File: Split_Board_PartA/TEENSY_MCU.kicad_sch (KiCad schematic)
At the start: 15 parts, among them J3 Conn_01x20, J4 Conn_01x15, U2 ADUM240E0BRWZ, U3 ADUM240E0BRWZ, U37 MYTEENSY_SYMBOL, U42 ADUM241E1BRIZ, U5 ADUM240E0BRWZ

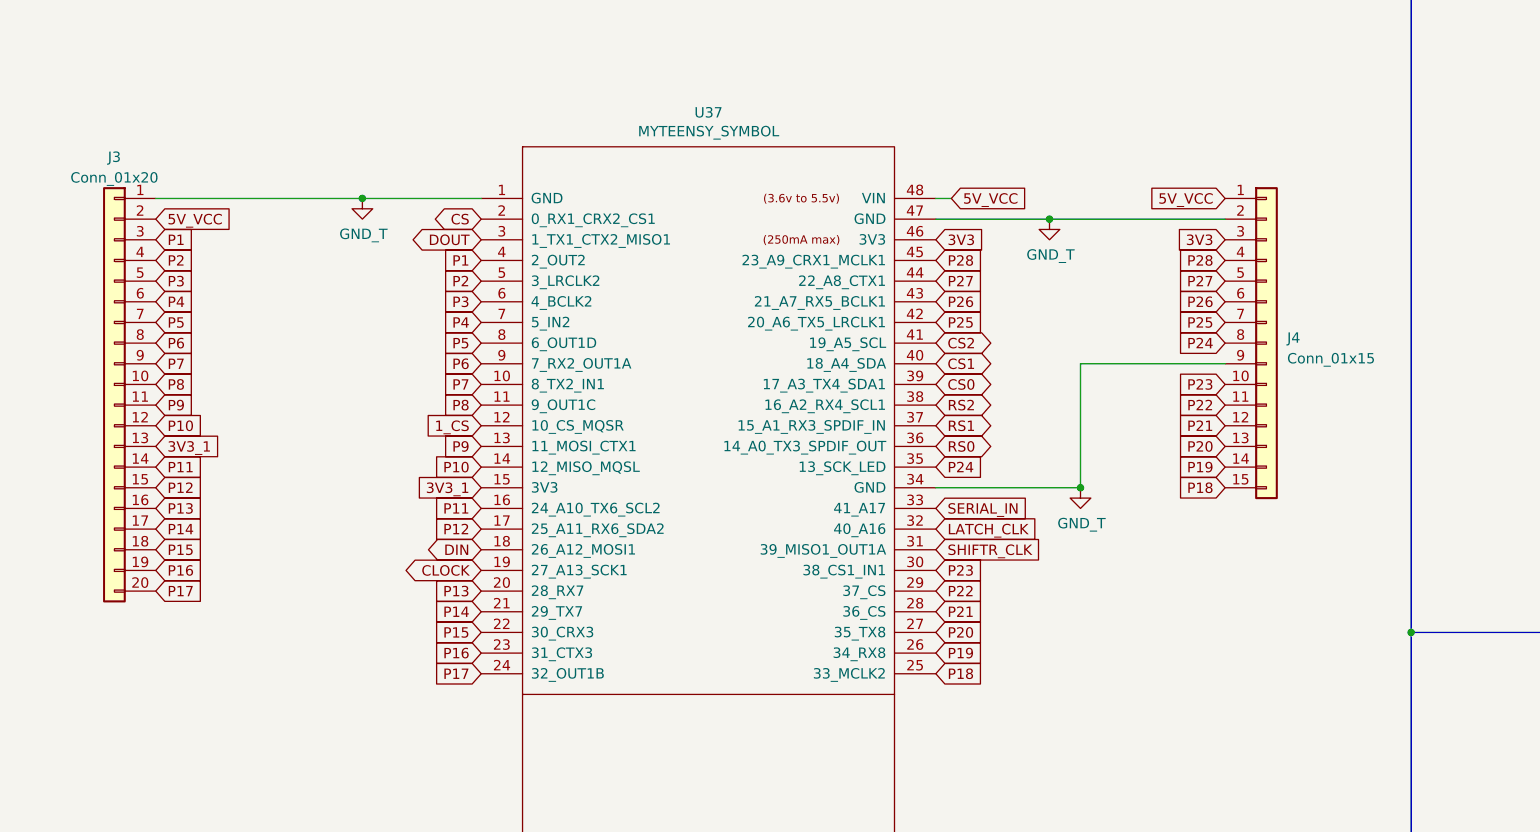
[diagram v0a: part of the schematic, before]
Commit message: edited the extra gpios of teensy
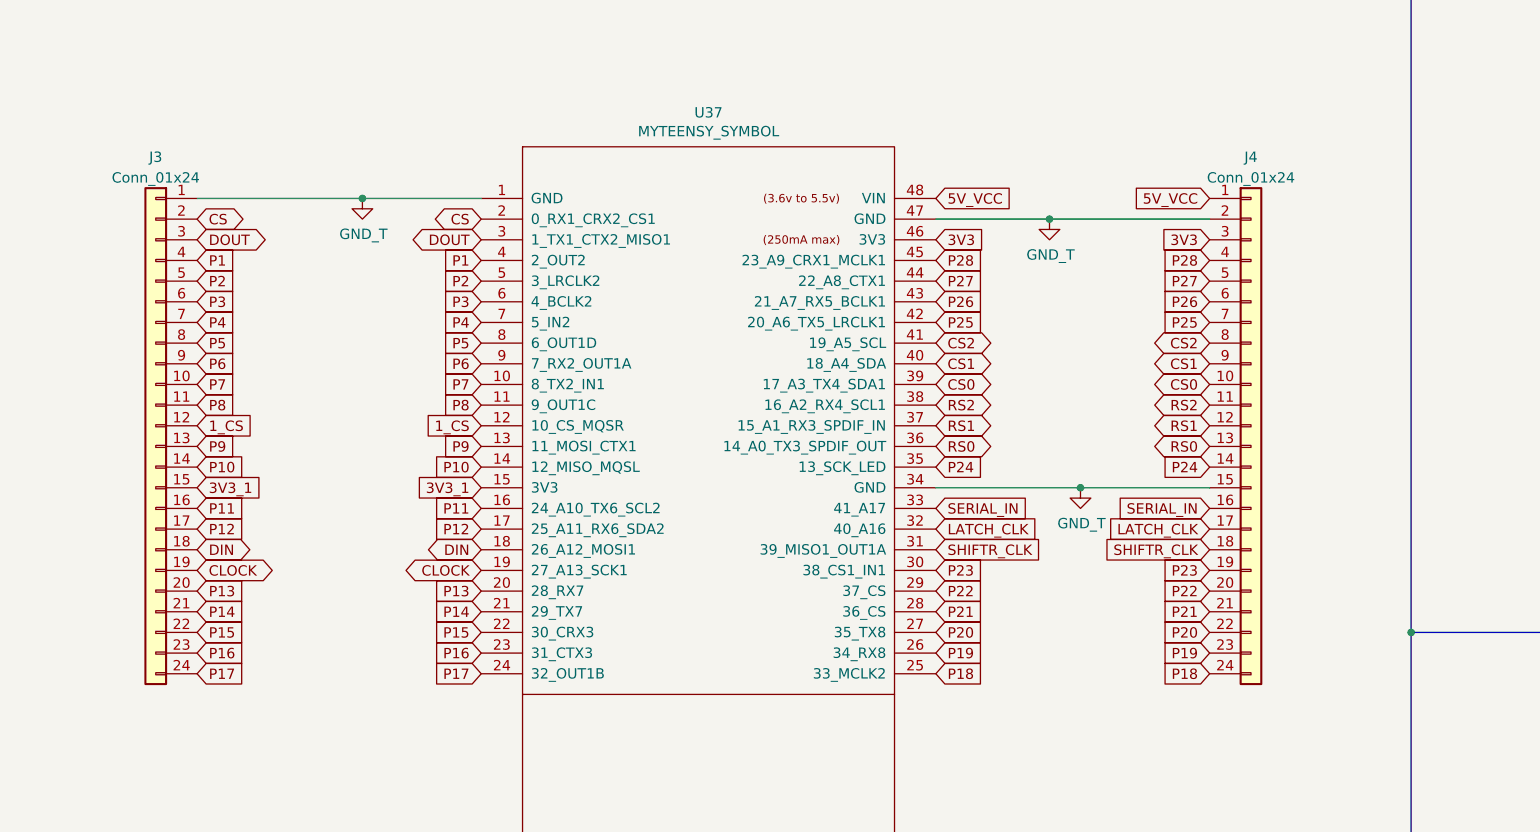
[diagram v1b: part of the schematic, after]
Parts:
- removed J3: Conn_01x20, symbol Connector_Generic:Conn_01x20
- removed J4: Conn_01x15, symbol Connector_Generic:Conn_01x15
- added J3, J4: Conn_01x24, symbol Connector_Generic:Conn_01x24
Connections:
- net 1_CS: now also J3.12 (Pin_12)
- net 3V3: now also J4.3 (Pin_3)
- net 3V3_1: now also J3.15 (Pin_15)
- net 5V_VCC: now also J4.1 (Pin_1)
- net CLOCK: now also J3.19 (Pin_19)
- net CS: now also J3.2 (Pin_2)
- net CS0: now also J4.10 (Pin_10)
- net CS1: now also J4.9 (Pin_9)
- net CS2: now also J4.8 (Pin_8)
- net DIN: now also J3.18 (Pin_18)
- net DOUT: now also J3.3 (Pin_3)
- net GND: now also J3.1 (Pin_1), J4.15 (Pin_15), J4.2 (Pin_2)
- net LATCH_CLK: now also J4.17 (Pin_17)
- net P1: now also J3.4 (Pin_4)
- net P10: now also J3.14 (Pin_14)
- net P11: now also J3.16 (Pin_16)
- net P12: now also J3.17 (Pin_17)
- net P13: now also J3.20 (Pin_20)
- net P14: now also J3.21 (Pin_21)
- net P15: now also J3.22 (Pin_22)
- net P16: now also J3.23 (Pin_23)
- net P17: now also J3.24 (Pin_24)
- net P18: now also J4.24 (Pin_24)
- net P19: now also J4.23 (Pin_23)
- net P2: now also J3.5 (Pin_5)
- net P20: now also J4.22 (Pin_22)
- net P21: now also J4.21 (Pin_21)
- net P22: now also J4.20 (Pin_20)
- net P23: now also J4.19 (Pin_19)
- net P24: now also J4.14 (Pin_14)
- net P25: now also J4.7 (Pin_7)
- net P26: now also J4.6 (Pin_6)
- net P27: now also J4.5 (Pin_5)
- net P28: now also J4.4 (Pin_4)
- net P3: now also J3.6 (Pin_6)
- net P4: now also J3.7 (Pin_7)
- net P5: now also J3.8 (Pin_8)
- net P6: now also J3.9 (Pin_9)
- net P7: now also J3.10 (Pin_10)
- net P8: now also J3.11 (Pin_11)
- net P9: now also J3.13 (Pin_13)
- net RS0: now also J4.13 (Pin_13)
- net RS1: now also J4.12 (Pin_12)
- net RS2: now also J4.11 (Pin_11)
- net SERIAL_IN: now also J4.16 (Pin_16)
- net SHIFTR_CLK: now also J4.18 (Pin_18)

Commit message: Removed the gerber files of espv5.0
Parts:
- J3, J4: footprint (none) -> Connector_PinHeader_2.54mm:PinHeader_1x24_P2.54mm_Vertical
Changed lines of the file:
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@@
       (effects (font (size 1.27 1.27)))
     )
-    (property "Footprint" "" (at 39.37 147.32 0)
+    (property "Footprint" "Connector_PinHeader_2.54mm:PinHeader_1x24_P2.54mm_Vertical" (at 39.37 147.32 0)
       (effects (font (size 1.27 1.27)) hide)
     )
@@
       (effects (font (size 1.27 1.27)))
     )
-    (property "Footprint" "" (at 173.99 147.32 0)
+    (property "Footprint" "Connector_PinHeader_2.54mm:PinHeader_1x24_P2.54mm_Vertical" (at 173.99 147.32 0)
       (effects (font (size 1.27 1.27)) hide)
     )

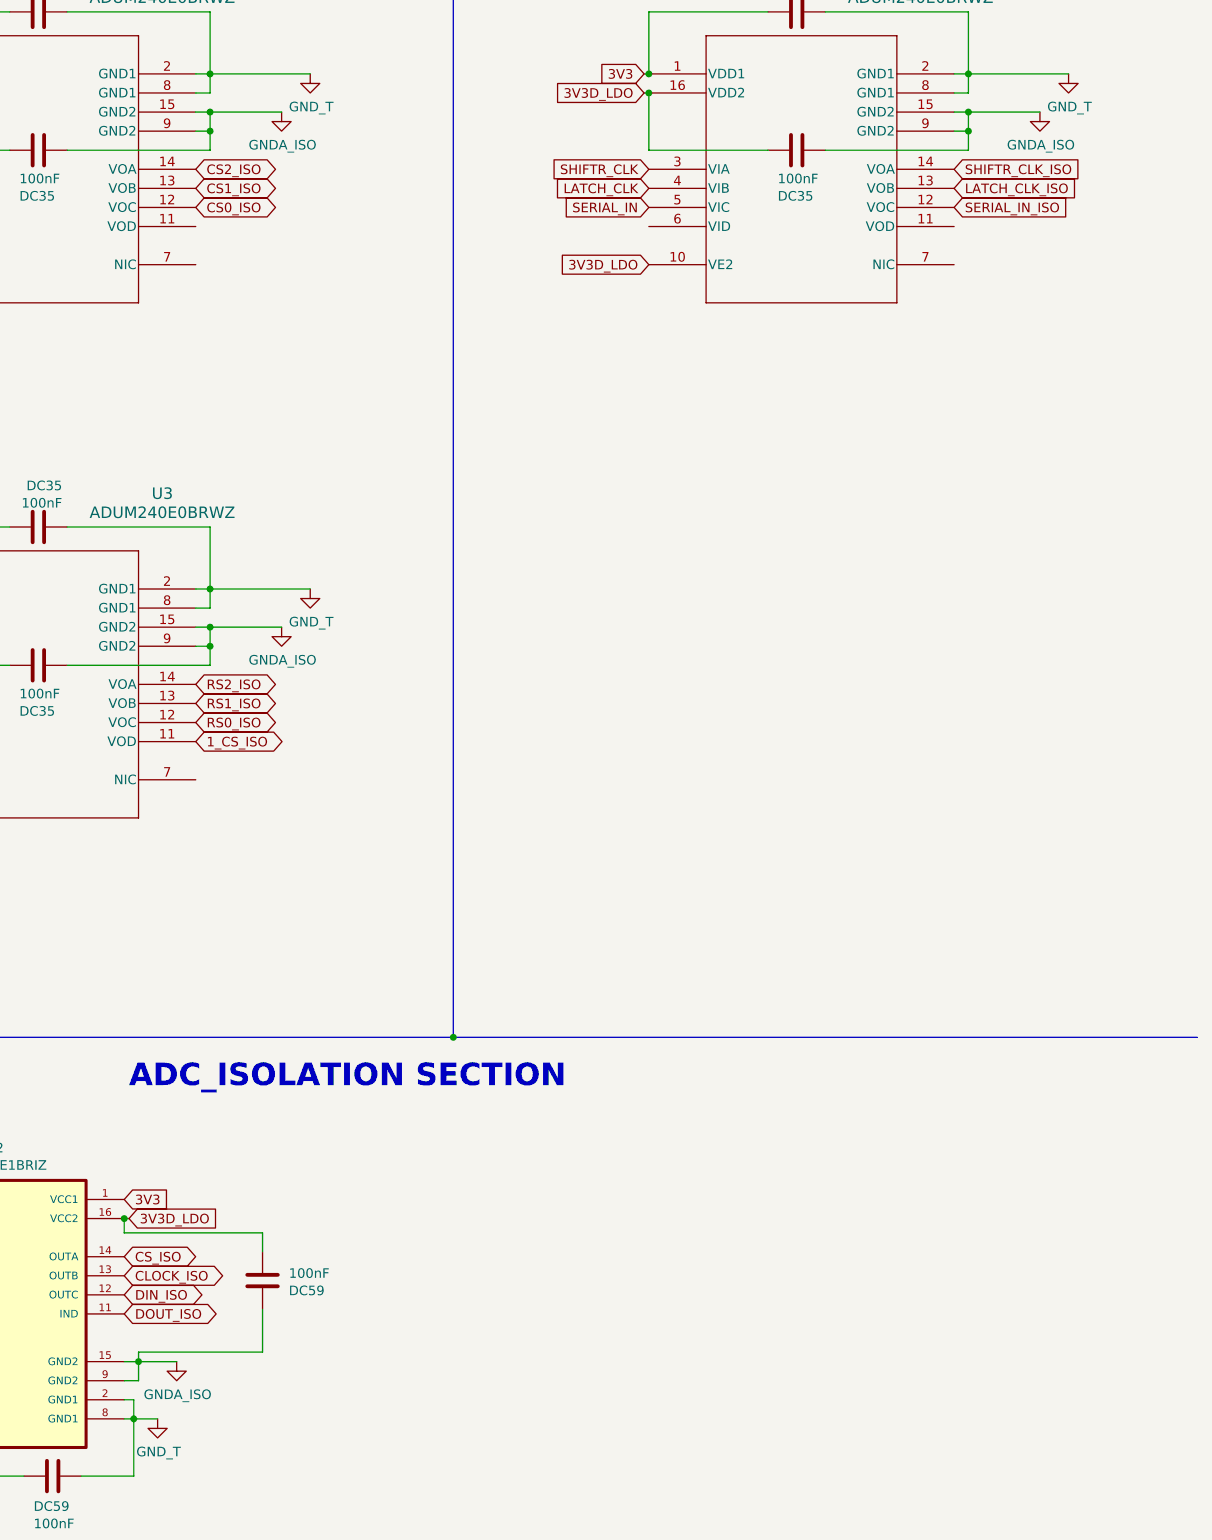
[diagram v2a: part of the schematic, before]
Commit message: changed the part A power section, added the ground GNDD_ISO
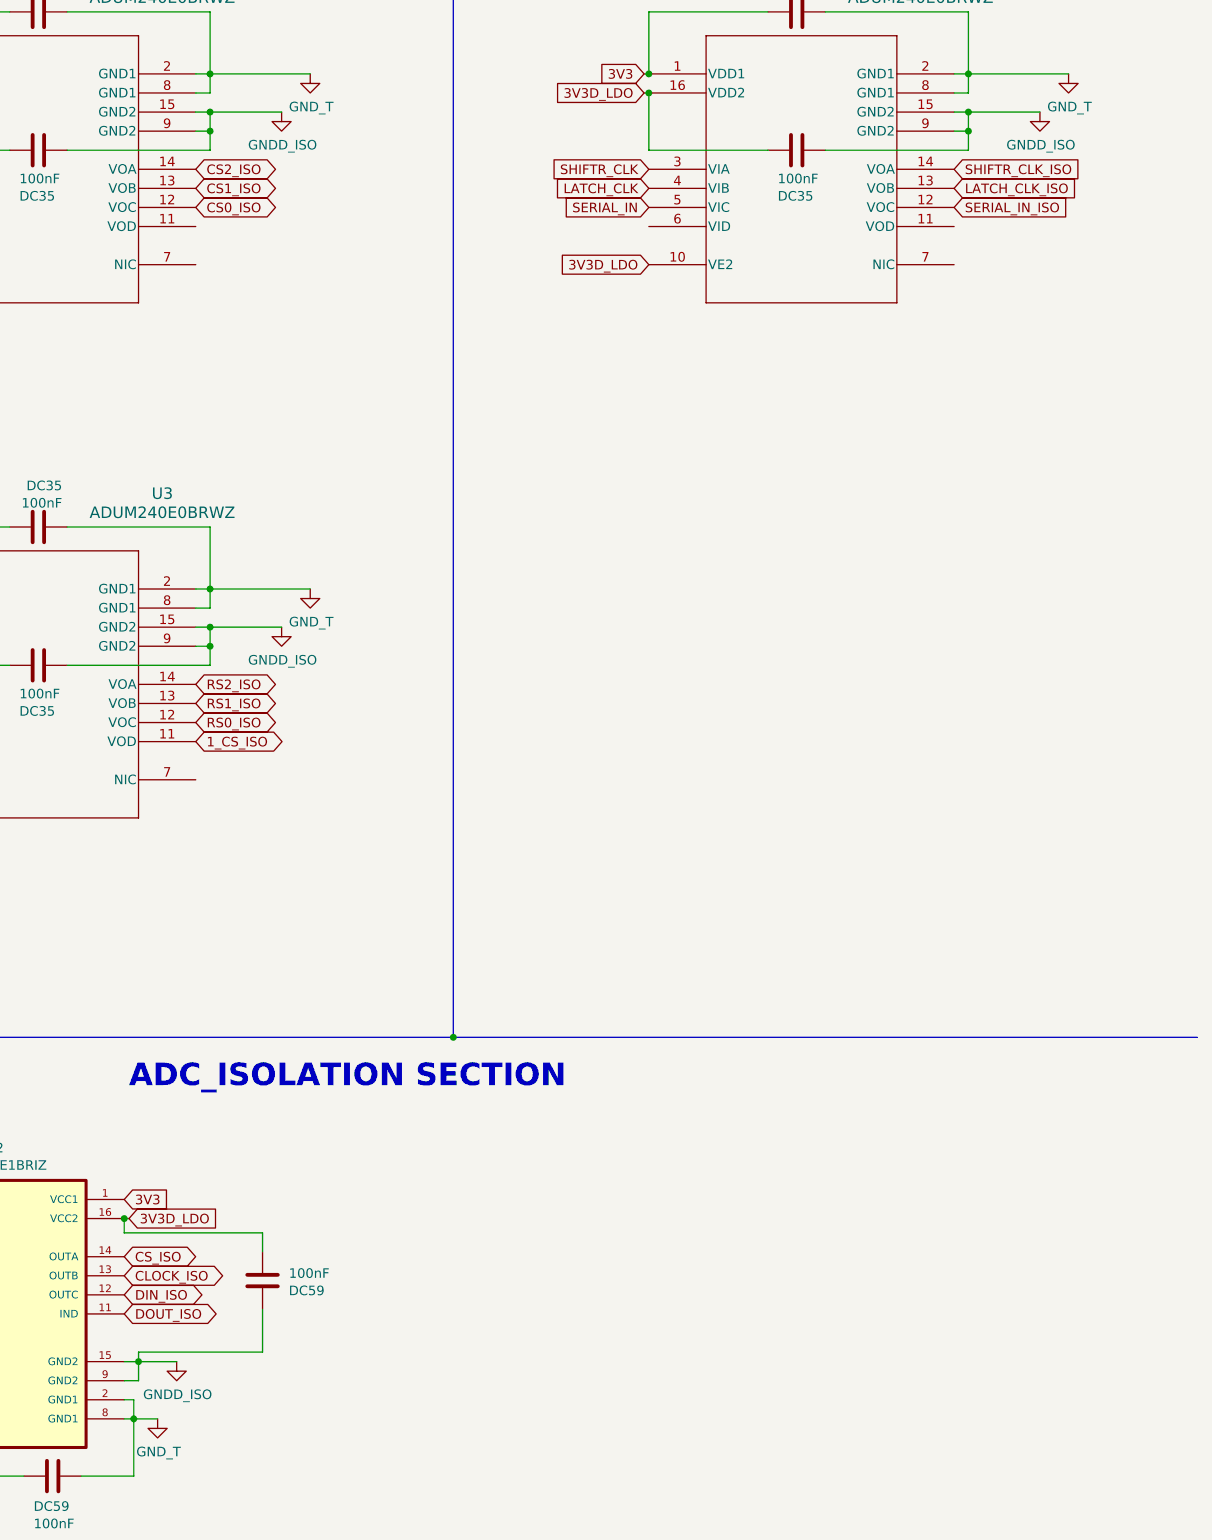
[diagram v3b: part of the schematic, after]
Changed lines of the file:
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@@
       (effects (font (size 1.27 1.27)) hide)
     )
-    (property "Value" "GNDA_ISO" (at 271.907 220.2942 0)
+    (property "Value" "GNDD_ISO" (at 271.907 220.2942 0)
       (effects (font (size 1.27 1.27)))
     )
@@
       (effects (font (size 1.27 1.27)) hide)
     )
-    (property "Value" "GNDA_ISO" (at 285.877 53.9242 0)
+    (property "Value" "GNDD_ISO" (at 285.877 53.9242 0)
       (effects (font (size 1.27 1.27)))
     )
@@
       (effects (font (size 1.27 1.27)) hide)
     )
-    (property "Value" "GNDA_ISO" (at 285.877 122.5042 0)
+    (property "Value" "GNDD_ISO" (at 285.877 122.5042 0)
       (effects (font (size 1.27 1.27)))
     )
@@
       (effects (font (size 1.27 1.27)) hide)
     )
-    (property "Value" "GNDA_ISO" (at 386.842 53.9242 0)
-      (effects (font (size 1.27 1.27)))
-    )
+    (property "Value" "GNDD_ISO" (at 386.842 53.9242 0)
+      (effects (font (size 1.27 1.27)))
+    )

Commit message: eliminated the GNDD_ISO net
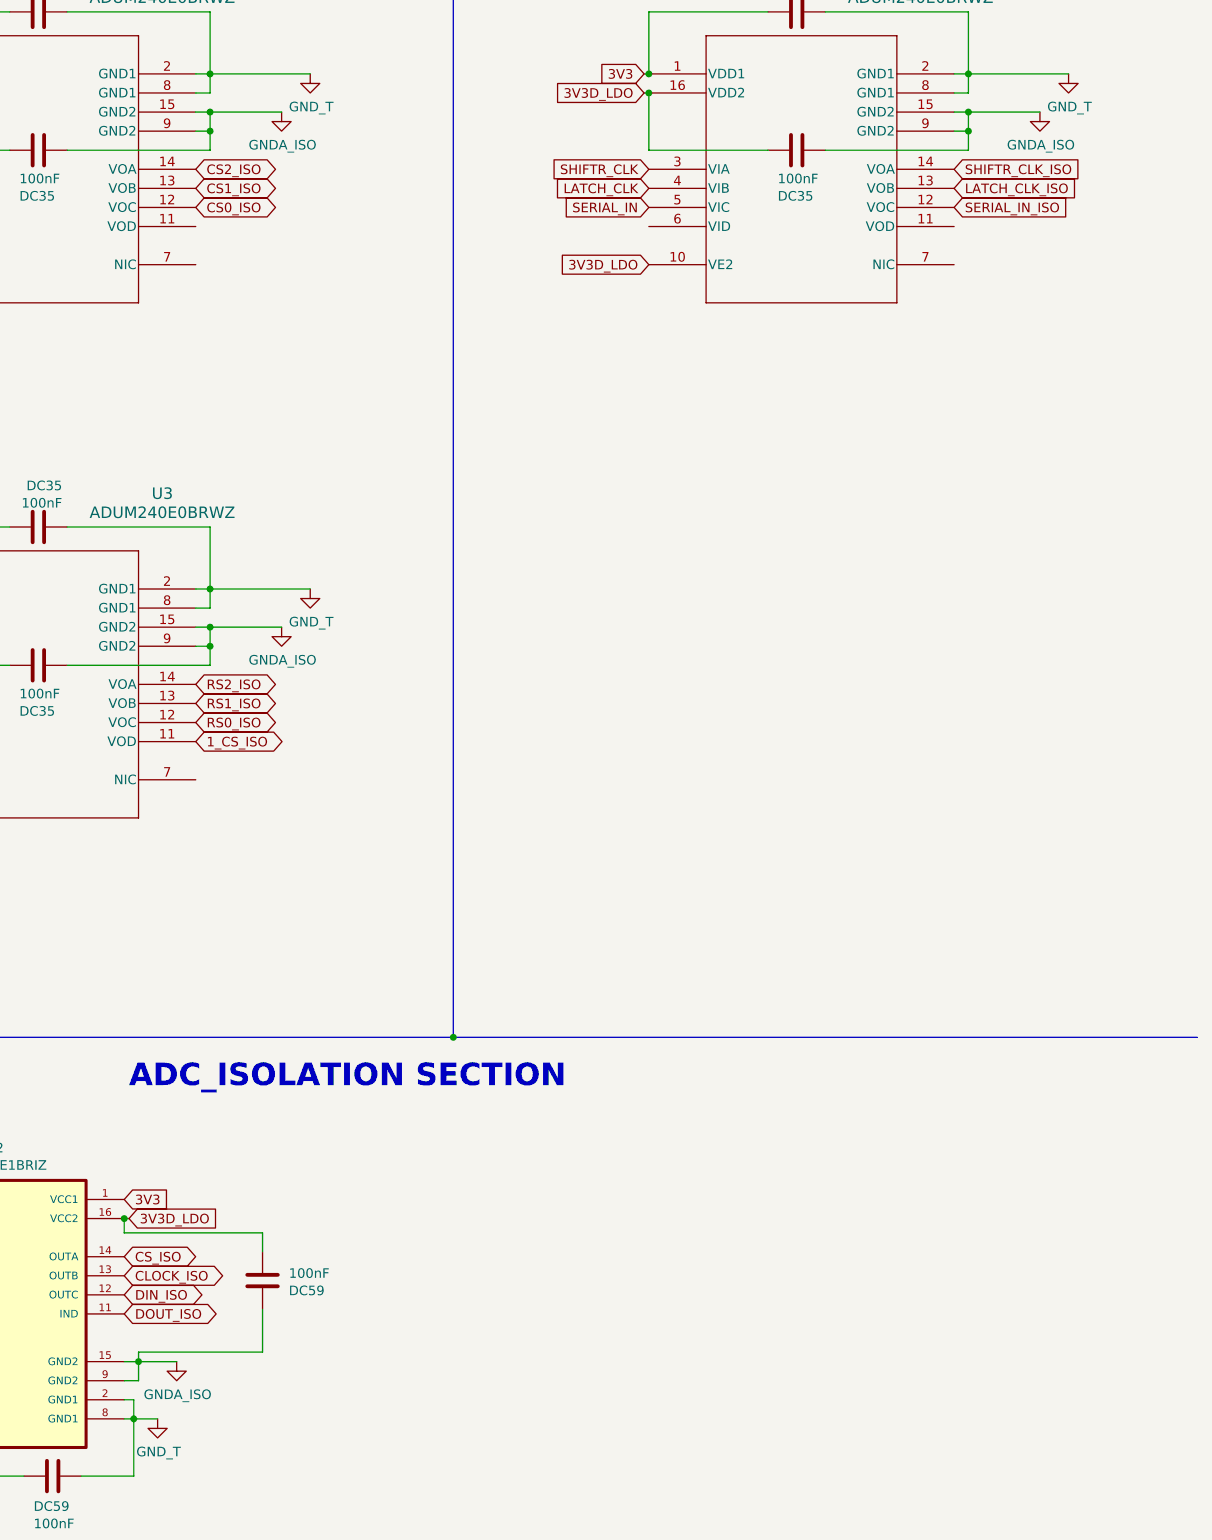
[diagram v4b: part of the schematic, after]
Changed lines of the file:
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@@
       (effects (font (size 1.27 1.27)) hide)
     )
-    (property "Value" "GNDD_ISO" (at 271.907 220.2942 0)
+    (property "Value" "GNDA_ISO" (at 271.907 220.2942 0)
       (effects (font (size 1.27 1.27)))
     )
@@
       (effects (font (size 1.27 1.27)) hide)
     )
-    (property "Value" "GNDD_ISO" (at 285.877 53.9242 0)
+    (property "Value" "GNDA_ISO" (at 285.877 53.9242 0)
       (effects (font (size 1.27 1.27)))
     )
@@
       (effects (font (size 1.27 1.27)) hide)
     )
-    (property "Value" "GNDD_ISO" (at 285.877 122.5042 0)
+    (property "Value" "GNDA_ISO" (at 285.877 122.5042 0)
       (effects (font (size 1.27 1.27)))
     )
@@
       (effects (font (size 1.27 1.27)) hide)
     )
-    (property "Value" "GNDD_ISO" (at 386.842 53.9242 0)
-      (effects (font (size 1.27 1.27)))
-    )
+    (property "Value" "GNDA_ISO" (at 386.842 53.9242 0)
+      (effects (font (size 1.27 1.27)))
+    )
